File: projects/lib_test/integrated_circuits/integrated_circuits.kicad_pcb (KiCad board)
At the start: 2 copper layers, 16 x 14 mm, 2 parts, among them U1001 LM393, U1002 AZ1117

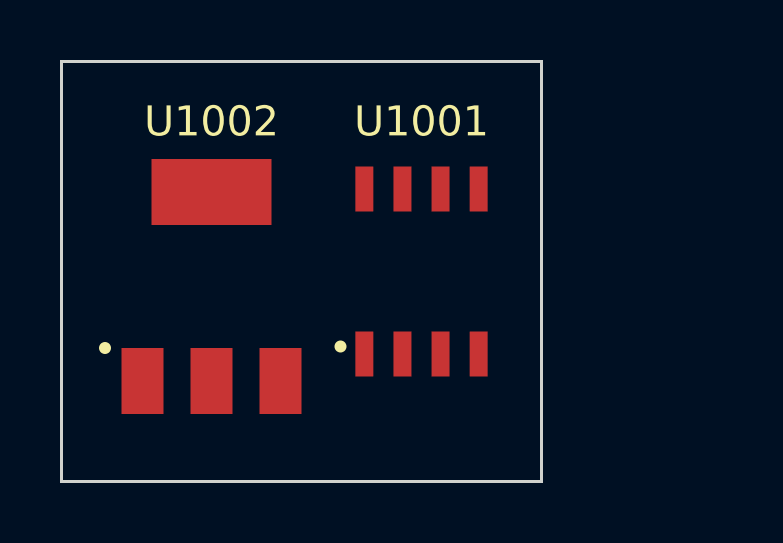
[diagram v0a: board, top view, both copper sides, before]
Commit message: add regulator TPS5430
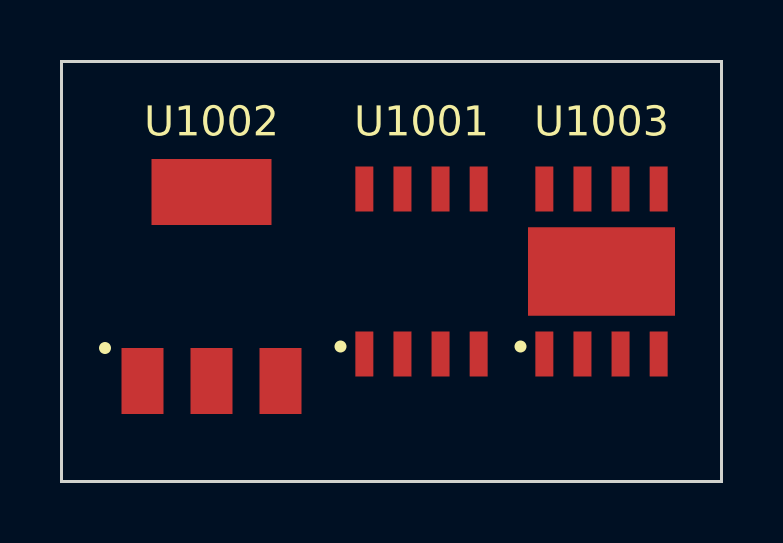
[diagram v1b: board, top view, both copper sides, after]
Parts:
- added U1003: TPS5430, lily_footprints:hsoic8, F.Cu at (138.0, 87.0)
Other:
- board size 16 x 14 mm -> 22 x 14 mm

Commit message: updated test projects
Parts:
- removed the U1002 at (125.0, 87.5)
- moved U1001 8.00 mm to (124.0, 87.0)
- moved U1002 7.00 mm to (131.0, 87.0)
- renumbered U1003 to U1002

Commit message: updated ic test project
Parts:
- removed U1001: LM393, lily_footprints:soic8
- removed U1002: TPS5430, lily_footprints:hsoic8
- added U10001: REF3040, lily_footprints:sot23, F.Cu at (176.6, 71.2)
- added U10002: AP2120N-3.3, lily_footprints:sot23, F.Cu at (176.6, 75.7)
- added U10003: AZ1117C, lily_footprints:sot223, F.Cu at (178.2, 87.5)
- added U10004: AP62200, lily_footprints:sot23-6_sc74, F.Cu at (176.6, 80.2)
- added U10005: TPS5430, lily_footprints:hsoic8, F.Cu at (182.3, 73.2)
- added U10006: TPS82130, lily_footprints:usip8_pitch0.65_2.8x3.0mm, F.Cu at (181.2, 79.7)
- added U10007: LM317, lily_footprints:to263-2, F.Cu at (167.2, 75.0)
- added U10008: LM337, lily_footprints:to263-2, F.Cu at (167.2, 87.1)
- added U11001: MCP6022, lily_footprints:soic8, F.Cu at (187.6, 124.2)
- added U11002: TLV272, lily_footprints:soic8, F.Cu at (194.1, 124.2)
- added U12001: NE555, lily_footprints:soic8, F.Cu at (216.1, 124.2)
- added U2001: ZXCT1010, lily_footprints:sot23-5, F.Cu at (206.4, 128.2)
- added U2002: LM335, lily_footprints:to92, F.Cu at (206.3, 123.4)
- added U2003: ADXL345, lily_footprints:lga14_pitch0.8_3x5mm, F.Cu at (201.7, 123.5)
- added U3001: LM393, lily_footprints:soic8, F.Cu at (215.5, 112.5)
- added U4001: DAC7311, lily_footprints:sot363-6_sc70-6, F.Cu at (206.4, 89.2)
- added U5001: 93LC56B, lily_footprints:sot23-6_sc74, F.Cu at (214.8, 104.1)
- added U5002: MX25L3233F, lily_footprints:soic8_5.3x5.3mm, F.Cu at (217.4, 98.5)
- added U6001: XC7A35T-XCSG325, lily_footprints:bga324_pitch0.8_15.0x15.0mm, F.Cu at (212.4, 77.2)
- added U7001: TXB0104, lily_footprints:uqfn12_pitch0.4_1.7x2.0mm, F.Cu at (179.3, 117.0)
- added U7002: SN75176B, lily_footprints:soic8, F.Cu at (174.2, 119.5)
- added U7003: TUSB4041I, lily_footprints:htqfp64_pitch0.5_10x10mm, F.Cu at (163.7, 102.3)
- added U7004: FT2232HL, lily_footprints:lqfp64_pitch0.5_10x10mm, F.Cu at (163.7, 116.8)
- added U7005: FT2232HQ, lily_footprints:qfn64_ep_pitch0.5mm_9x9mm, F.Cu at (176.7, 100.8)
- added U7006: FT231XS, lily_footprints:ssop20_pitch25_341x154mil, F.Cu at (176.1, 110.9)
- added U8001: ESP32-C3FH4, lily_footprints:qfn32_ep_pitch0.5mm_5x5mm, F.Cu at (199.5, 113.2)
- added U8002: ATMEGA32A, lily_footprints:tqfp44_pitch0.8_10x10mm, F.Cu at (203.1, 102.3)
- added U8003: ATMEGA168PB, lily_footprints:tqfp32_pitch0.8_7x7mm, F.Cu at (190.1, 100.8)
- added U8004: ATMEGA328PB, lily_footprints:tqfp32_pitch0.8_7x7mm, F.Cu at (190.1, 112.3)
- added U9001: ESP32-C3-MINI-1, lily_footprints:esp32_c3_mini_1, F.Cu at (194.9, 80.8)

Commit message: updated test projects
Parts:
- added U1020: ESP32-C6-MINI-1, lily_footprints:esp32_c3_mini_1, F.Cu at (153.0, 56.0)
- added U1021: RFM95W-868S2, lily_footprints:rfm95w-868s2, F.Cu at (171.0, 60.0)
- added U1033: BQ24073, lily_footprints:vqfn16_ep_pitch0.5_3.1x3.1mm, F.Cu at (144.0, 109.0)
- moved U1005 89.6 mm to (119.0, 109.0), turned to -90 degrees
- moved U1006 85.9 mm to (129.0, 109.0), turned to -90 degrees
- moved U1003 82.1 mm to (120.0, 116.0), turned to 90 degrees
- moved U1001 81.7 mm to (129.0, 102.0)
- moved U1016 81.0 mm to (123.0, 90.0)
- moved U1012 71.5 mm to (123.0, 58.0)
- moved U1007 67.1 mm to (151.0, 108.0), turned to 90 degrees
- moved U1022 65.3 mm to (119.0, 102.0)
- moved U1019 62.0 mm to (138.0, 56.0)
- moved U1025 60.0 mm to (124.0, 109.0), turned to -90 degrees
- moved U1008 59.7 mm to (153.0, 72.0)
- moved U1023 58.8 mm to (124.0, 102.0)
- moved U1004 57.7 mm to (158.0, 108.0)
- moved U1015 57.4 mm to (149.0, 86.0)
- moved U1027 55.6 mm to (134.0, 109.0)
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- renumbered U2001 to U1001, U2002 to U1002, U2003 to U1003, U3001 to U1004, U4001 to U1005, U5001 to U1006, U5002 to U1007, U6001 to U1008, U7001 to U1009, U7002 to U1010, U7003 to U1011, U7004 to U1012, U7005 to U1013, U7006 to U1014, U8001 to U1015, U8002 to U1016, U8003 to U1017, U8004 to U1018, U9001 to U1019, U10001 to U1022, U10002 to U1023, U10003 to U1024, U10004 to U1025, U10005 to U1026, U10006 to U1027, U10007 to U1028, U10008 to U1029, U11001 to U1030, U11002 to U1031, U12001 to U1032
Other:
- board size 22 x 14 mm -> 70 x 79 mm

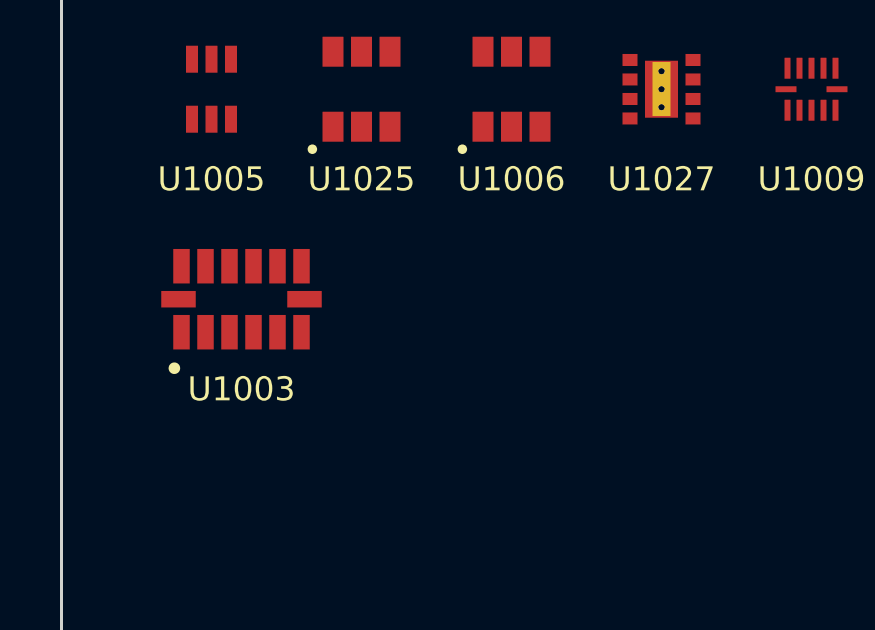
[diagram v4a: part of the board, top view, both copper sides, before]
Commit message: add AT24QT1010 to test design
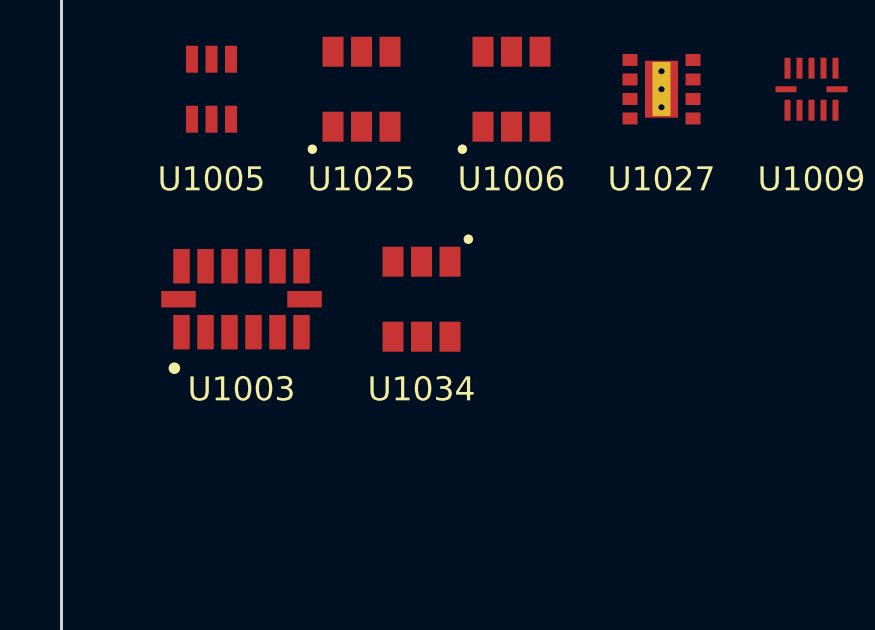
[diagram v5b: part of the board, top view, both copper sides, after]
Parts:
- added U1034: AT24QT1010, lily_footprints:sot23-6_sc74, F.Cu at (126.0, 116.0)
